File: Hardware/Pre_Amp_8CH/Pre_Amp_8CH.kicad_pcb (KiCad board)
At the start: 2 copper layers, 200 x 75 mm, 5 parts, among them J1 PJRAS4X2U01AUX, J2 PJRAS4X2U01AUX, J3 USB_C_Receptacle_PowerOnly_6P

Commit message: DSP start
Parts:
- added IC501: STA309A13TR, Pre_Amp_8CH_Footprints:QFP50P1200X1200X160-64N, F.Cu at (179.1, 120.0)
- added U601: STM32F410R8Tx, Package_QFP:LQFP-64_10x10mm_P0.5mm, F.Cu at (104.1, 120.0)
- renumbered J3 to J201, J1 to J301, J2 to J401, R1 to R201, R2 to R202
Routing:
- net /PSU/VBUS: track 0.00 -> 7.23 mm
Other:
- outline, holes or cut-outs redrawn

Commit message: PSU
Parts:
- added C201: 865060240001, Pre_Amp_8CH_Footprints:CP_Wurth_WCAP-ASLL-D4L5.5, F.Cu at (67.6, 97.3)
- added C202: 865060240001, Pre_Amp_8CH_Footprints:CP_Wurth_WCAP-ASLL-D4L5.5, F.Cu at (76.7, 107.9)
- added C501: 100nF, Capacitor_SMD:C_0603_1608Metric_Pad1.08x0.95mm_HandSolder, F.Cu at (183.0, 130.0)
- added C502: 1nF, Capacitor_SMD:C_0603_1608Metric_Pad1.08x0.95mm_HandSolder, F.Cu at (195.5, 131.6)
- added C503: 100nF, Capacitor_SMD:C_0603_1608Metric_Pad1.08x0.95mm_HandSolder, F.Cu at (168.8, 123.7)
- added C504: 100nF, Capacitor_SMD:C_0603_1608Metric_Pad1.08x0.95mm_HandSolder, F.Cu at (190.2, 122.7)
- added C505: 100nF, Capacitor_SMD:C_0603_1608Metric_Pad1.08x0.95mm_HandSolder, F.Cu at (189.9, 117.6)
- added C506: 100nF, Capacitor_SMD:C_0603_1608Metric_Pad1.08x0.95mm_HandSolder, F.Cu at (181.8, 109.7)
- added C507: 100nF, Capacitor_SMD:C_0603_1608Metric_Pad1.08x0.95mm_HandSolder, F.Cu at (177.2, 109.2)
- added C508: 1n2, Capacitor_SMD:C_0603_1608Metric_Pad1.08x0.95mm_HandSolder, F.Cu at (180.7, 137.8)
- added C509: 2u2, Capacitor_SMD:C_0805_2012Metric_Pad1.18x1.45mm_HandSolder, F.Cu at (168.5, 107.8)
- added C510: 100nF, Capacitor_SMD:C_0603_1608Metric_Pad1.08x0.95mm_HandSolder, F.Cu at (168.5, 110.8)
- added C511: 100p, Capacitor_SMD:C_0603_1608Metric_Pad1.08x0.95mm_HandSolder, F.Cu at (179.8, 133.7)
- added C512: 100p, Capacitor_SMD:C_0603_1608Metric_Pad1.08x0.95mm_HandSolder, F.Cu at (179.0, 128.7)
- added C513: 100nF, Capacitor_SMD:C_0603_1608Metric_Pad1.08x0.95mm_HandSolder, F.Cu at (205.1, 134.6)
- added C514: 47p, Capacitor_SMD:C_0603_1608Metric_Pad1.08x0.95mm_HandSolder, F.Cu at (165.8, 121.7)
- added C515: 1nF, Capacitor_SMD:C_0603_1608Metric_Pad1.08x0.95mm_HandSolder, F.Cu at (201.5, 122.7)
- added FB501: 600ohm100MHz, Resistor_SMD:R_0805_2012Metric_Pad1.20x1.40mm_HandSolder, F.Cu at (183.9, 136.8)
- added JP201: USB_jumper, Jumper:SolderJumper-2_P1.3mm_Open_Pad1.0x1.5mm, F.Cu at (65.8, 89.3)
- added JP202: 3V3_jumper, Jumper:SolderJumper-2_P1.3mm_Open_Pad1.0x1.5mm, F.Cu at (80.6, 113.2)
- added L201: BMRA000606301R0MA1, Pre_Amp_8CH_Footprints:INDPM7366X300N, F.Cu at (68.7, 109.7)
- added R203: 453k, Resistor_SMD:R_0603_1608Metric_Pad0.98x0.95mm_HandSolder, F.Cu at (72.8, 102.7)
- added R204: 100k, Resistor_SMD:R_0603_1608Metric_Pad0.98x0.95mm_HandSolder, F.Cu at (69.8, 102.7)
- added R501: 3K4, Resistor_SMD:R_0603_1608Metric_Pad0.98x0.95mm_HandSolder, F.Cu at (177.0, 133.7)
- added R502: 10K, Resistor_SMD:R_0603_1608Metric_Pad0.98x0.95mm_HandSolder, F.Cu at (168.1, 131.9)
- added R503: 10K, Resistor_SMD:R_0603_1608Metric_Pad0.98x0.95mm_HandSolder, F.Cu at (171.0, 131.9)
- added TP201: USB, TestPoint:TestPoint_Pad_D1.0mm, F.Cu at (65.8, 86.0)
- added TP202: 3V3, TestPoint:TestPoint_Pad_D1.0mm, F.Cu at (76.7, 113.2)
- added U201: TLV62569ADRL, Package_TO_SOT_SMD:SOT-563, F.Cu at (66.3, 104.2)
- R201, R202: footprint Resistor_SMD:R_0805_2012Metric_Pad1.20x1.40mm_HandSolder -> Resistor_SMD:R_0603_1608Metric_Pad0.98x0.95mm_HandSolder
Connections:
- IC501 pad 1: unconnected-(IC501-MVO-Pad1) -> +3V3
- IC501 pad 10: unconnected-(IC501-LRCKI-Pad10) -> /Audio_DSP/LRCKI
- IC501 pad 11: unconnected-(IC501-BICKI-Pad11) -> /Audio_DSP/BICKI
- IC501 pad 15: unconnected-(IC501-RESET-Pad15) -> /Audio_DSP/POWER_ON_RESET
- IC501 pad 16: unconnected-(IC501-PLLB-Pad16) -> GNDD
- IC501 pad 17: unconnected-(IC501-SA-Pad17) -> GNDD
- IC501 pad 20: unconnected-(IC501-XTI-Pad20) -> /Audio_DSP/MCLK
- IC501 pad 21: unconnected-(IC501-FILTER_PLL-Pad21) -> /Audio_DSP/PLL-Filter
- IC501 pad 23: unconnected-(IC501-GNDA-Pad23) -> /Audio_DSP/PLL-Filter-GND
- IC501 pad 24: unconnected-(IC501-VDDA-Pad24) -> Net-(IC501-VDDA)
- IC501 pad 25: unconnected-(IC501-CKOUT-Pad25) -> /Audio_DSP/CKOUT
- IC501 pad 29: unconnected-(IC501-OUT8_B-Pad29) -> /Audio_DSP/OUT8_B
- IC501 pad 30: unconnected-(IC501-OUT8_A-Pad30) -> /Audio_DSP/OUT8_A
- IC501 pad 31: unconnected-(IC501-OUT7_B-Pad31) -> /Audio_DSP/OUT7_B
- IC501 pad 32: unconnected-(IC501-OUT7_A-Pad32) -> /Audio_DSP/OUT7_A
- IC501 pad 33: unconnected-(IC501-OUT6_B-Pad33) -> /Audio_DSP/OUT6_B
- IC501 pad 34: unconnected-(IC501-OUT6_A-Pad34) -> /Audio_DSP/OUT6_A
- IC501 pad 38: unconnected-(IC501-OUT5_B-Pad38) -> /Audio_DSP/OUT5_B
- IC501 pad 39: unconnected-(IC501-OUT5_A-Pad39) -> /Audio_DSP/OUT5_A
- IC501 pad 40: unconnected-(IC501-OUT4_B-Pad40) -> /Audio_DSP/OUT4_B
- IC501 pad 41: unconnected-(IC501-OUT4_A-Pad41) -> /Audio_DSP/OUT4_A
- IC501 pad 42: unconnected-(IC501-OUT3_B-Pad42) -> /Audio_DSP/OUT3_B
- IC501 pad 43: unconnected-(IC501-OUT3_A-Pad43) -> /Audio_DSP/OUT3_A
- IC501 pad 47: unconnected-(IC501-OUT2_B-Pad47) -> /Audio_DSP/OUT2_B
- IC501 pad 48: unconnected-(IC501-OUT2_A-Pad48) -> /Audio_DSP/OUT2_A
- IC501 pad 49: unconnected-(IC501-OUT1_B-Pad49) -> /Audio_DSP/OUT1_B
- IC501 pad 50: unconnected-(IC501-OUT1_A-Pad50) -> /Audio_DSP/OUT1_A
- IC501 pad 51: unconnected-(IC501-EAPD-Pad51) -> /Audio_DSP/EAPD
- IC501 pad 55: unconnected-(IC501-BICKO-Pad55) -> /Audio_DSP/BICKO
- IC501 pad 56: unconnected-(IC501-LRCKO-Pad56) -> /Audio_DSP/LRCKO
- IC501 pad 57: unconnected-(IC501-SDO_12-Pad57) -> /Audio_DSP/SDATA_OUT_12
- IC501 pad 58: unconnected-(IC501-SDO_34-Pad58) -> /Audio_DSP/SDATA_OUT_34
- IC501 pad 6: unconnected-(IC501-SDI_78-Pad6) -> /Audio_DSP/SDATA_IN_78
- IC501 pad 62: unconnected-(IC501-SDO_56-Pad62) -> /Audio_DSP/SDATA_OUT_56
- IC501 pad 63: unconnected-(IC501-SDO_78-Pad63) -> /Audio_DSP/SDATA_OUT_78
- IC501 pad 64: unconnected-(IC501-PWDN-Pad64) -> /Audio_DSP/PWDN
- IC501 pad 7: unconnected-(IC501-SDI_56-Pad7) -> /Audio_DSP/SDATA_IN_56
- IC501 pad 8: unconnected-(IC501-SDI_34-Pad8) -> /Audio_DSP/SDATA_IN_34
- IC501 pad 9: unconnected-(IC501-SDI_12-Pad9) -> /Audio_DSP/SDATA_IN_12
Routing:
- net /Audio_DSP/I2C_SDA: track 0.00 -> 12.4 mm
- net /PSU/VBUS: track 7.23 -> 17.8 mm
- net /Audio_DSP/I2C_SCL: track 0.00 -> 9.84 mm
- net +5V: track 0.00 -> 8.98 mm
- net /PSU/FB: track 0.00 -> 7.03 mm
- net +3V3: track 0.00 -> 2.95 mm, vias 0 -> 4
- net GNDD: track 0.00 -> 2.31 mm, vias 2 -> 16
- added copper zone on F.Cu, net +5V
- added copper zone on F.Cu, net /PSU/3V3_sb
- added copper zone on F.Cu, net /PSU/SW
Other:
- outline, holes or cut-outs redrawn
- copper layers 2 -> 4

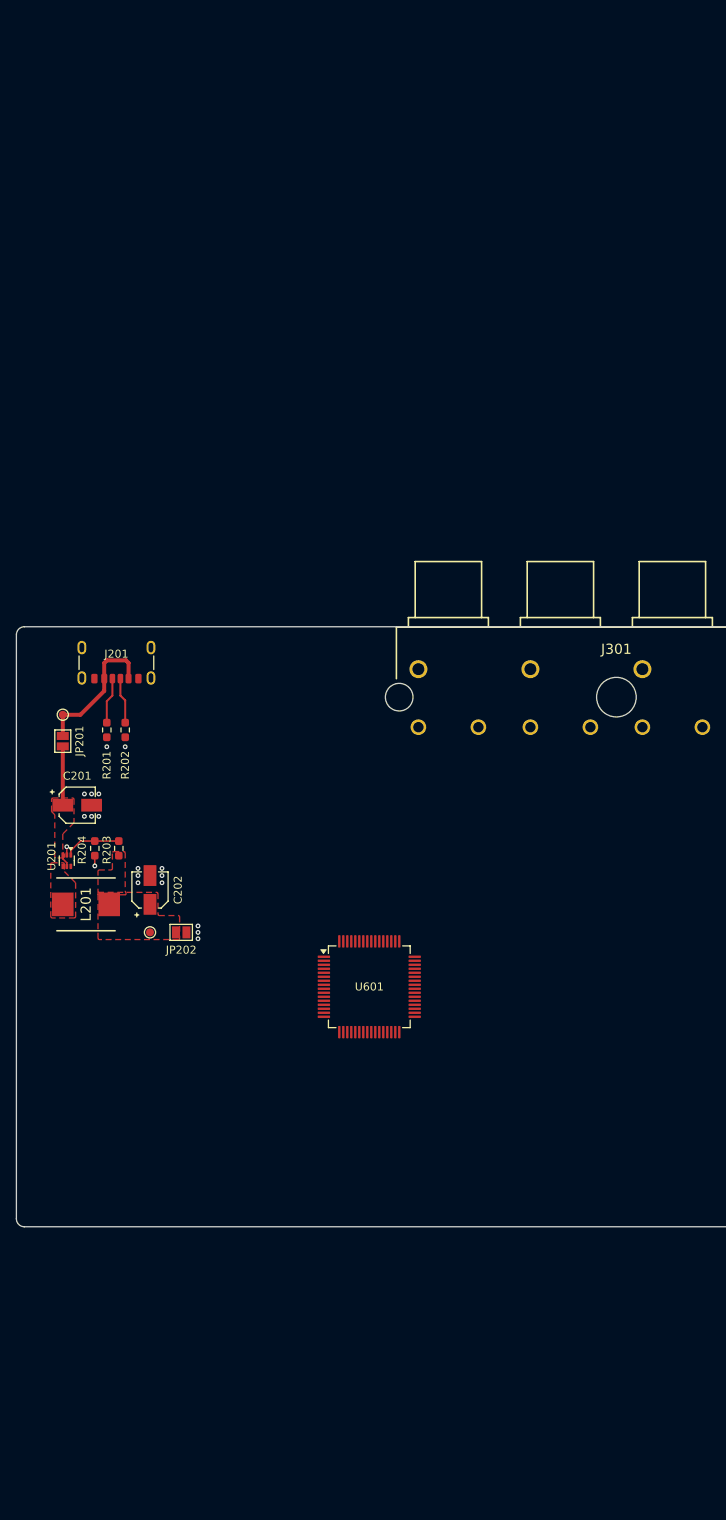
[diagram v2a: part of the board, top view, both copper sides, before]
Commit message: audio input buffers
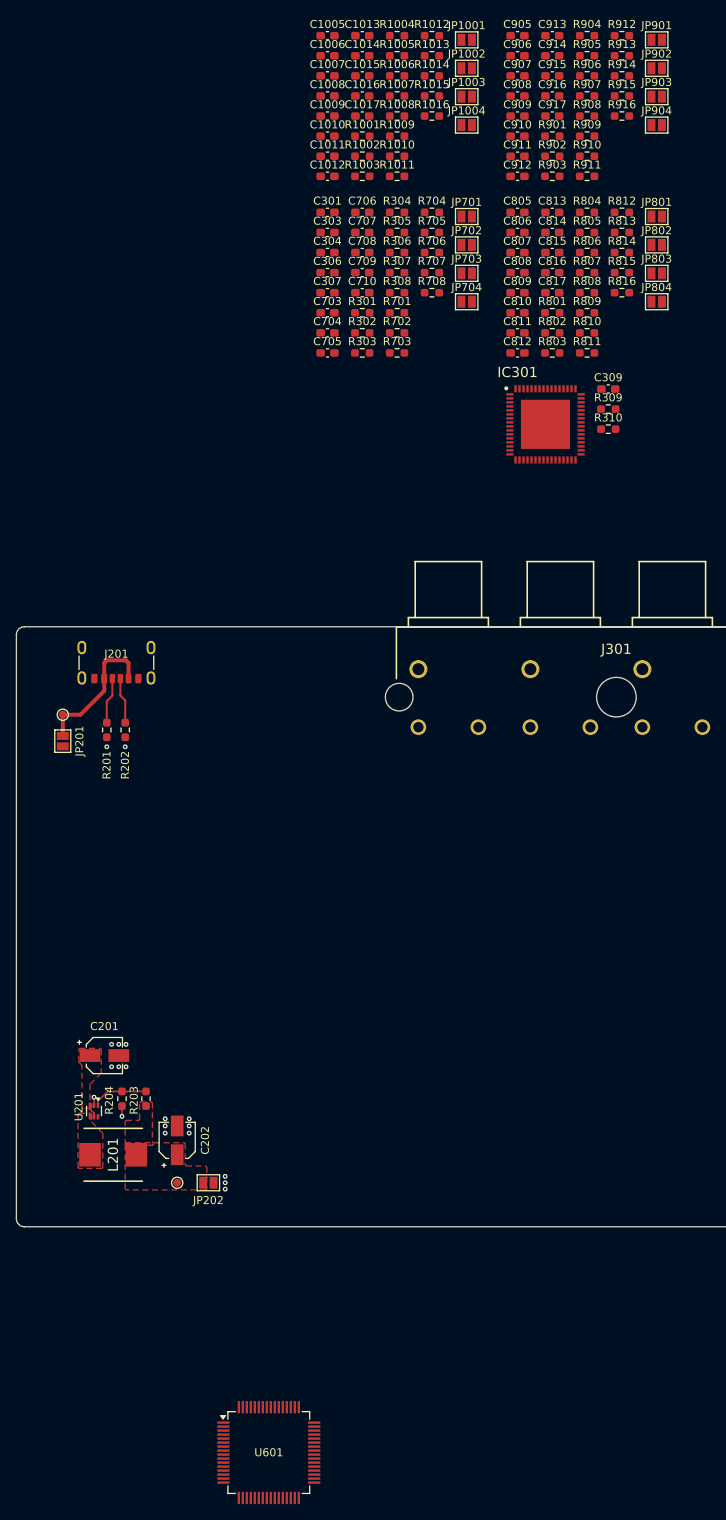
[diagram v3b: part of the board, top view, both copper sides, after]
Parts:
- added C1005: 1n_film, Capacitor_SMD:C_0603_1608Metric_Pad1.08x0.95mm_HandSolder, F.Cu at (98.9, 1.12)
- added C1006: 1n_film, Capacitor_SMD:C_0603_1608Metric_Pad1.08x0.95mm_HandSolder, F.Cu at (98.9, 3.63)
- added C1007: 1n_film, Capacitor_SMD:C_0603_1608Metric_Pad1.08x0.95mm_HandSolder, F.Cu at (98.9, 6.14)
- added C1008: 1n_film, Capacitor_SMD:C_0603_1608Metric_Pad1.08x0.95mm_HandSolder, F.Cu at (98.9, 8.65)
- added C1009: 100p, Capacitor_SMD:C_0603_1608Metric_Pad1.08x0.95mm_HandSolder, F.Cu at (98.9, 11.2)
- added C1010: 100p, Capacitor_SMD:C_0603_1608Metric_Pad1.08x0.95mm_HandSolder, F.Cu at (98.9, 13.7)
- added C1011: 100p, Capacitor_SMD:C_0603_1608Metric_Pad1.08x0.95mm_HandSolder, F.Cu at (98.9, 16.2)
- added C1012: 100p, Capacitor_SMD:C_0603_1608Metric_Pad1.08x0.95mm_HandSolder, F.Cu at (98.9, 18.7)
- added C1013: 15n_film, Capacitor_SMD:C_0603_1608Metric_Pad1.08x0.95mm_HandSolder, F.Cu at (103.2, 1.12)
- added C1014: 15n_film, Capacitor_SMD:C_0603_1608Metric_Pad1.08x0.95mm_HandSolder, F.Cu at (103.2, 3.63)
- added C1015: 100n, Capacitor_SMD:C_0603_1608Metric_Pad1.08x0.95mm_HandSolder, F.Cu at (103.2, 6.14)
- added C1016: 100n, Capacitor_SMD:C_0603_1608Metric_Pad1.08x0.95mm_HandSolder, F.Cu at (103.2, 8.65)
- added C1017: 100n, Capacitor_SMD:C_0603_1608Metric_Pad1.08x0.95mm_HandSolder, F.Cu at (103.2, 11.2)
- added C301: 1n_film, Capacitor_SMD:C_0603_1608Metric_Pad1.08x0.95mm_HandSolder, F.Cu at (98.9, 23.2)
- added C303: 100p, Capacitor_SMD:C_0603_1608Metric_Pad1.08x0.95mm_HandSolder, F.Cu at (98.9, 25.7)
- added C304: 15n_film, Capacitor_SMD:C_0603_1608Metric_Pad1.08x0.95mm_HandSolder, F.Cu at (98.9, 28.2)
- added C306: 1n_film, Capacitor_SMD:C_0603_1608Metric_Pad1.08x0.95mm_HandSolder, F.Cu at (98.9, 30.7)
- added C307: 100p, Capacitor_SMD:C_0603_1608Metric_Pad1.08x0.95mm_HandSolder, F.Cu at (98.9, 33.2)
- added C309: 100n, Capacitor_SMD:C_0603_1608Metric_Pad1.08x0.95mm_HandSolder, F.Cu at (134.0, 45.3)
- added C703: 1n_film, Capacitor_SMD:C_0603_1608Metric_Pad1.08x0.95mm_HandSolder, F.Cu at (98.9, 35.8)
- added C704: 1n_film, Capacitor_SMD:C_0603_1608Metric_Pad1.08x0.95mm_HandSolder, F.Cu at (98.9, 38.3)
- added C705: 100p, Capacitor_SMD:C_0603_1608Metric_Pad1.08x0.95mm_HandSolder, F.Cu at (98.9, 40.8)
- added C706: 100p, Capacitor_SMD:C_0603_1608Metric_Pad1.08x0.95mm_HandSolder, F.Cu at (103.2, 23.2)
- added C707: 15n_film, Capacitor_SMD:C_0603_1608Metric_Pad1.08x0.95mm_HandSolder, F.Cu at (103.2, 25.7)
- added C708: 100n, Capacitor_SMD:C_0603_1608Metric_Pad1.08x0.95mm_HandSolder, F.Cu at (103.2, 28.2)
- added C709: 100n, Capacitor_SMD:C_0603_1608Metric_Pad1.08x0.95mm_HandSolder, F.Cu at (103.2, 30.7)
- added C710: 100n, Capacitor_SMD:C_0603_1608Metric_Pad1.08x0.95mm_HandSolder, F.Cu at (103.2, 33.2)
- added C805: 1n_film, Capacitor_SMD:C_0603_1608Metric_Pad1.08x0.95mm_HandSolder, F.Cu at (122.6, 23.2)
- added C806: 1n_film, Capacitor_SMD:C_0603_1608Metric_Pad1.08x0.95mm_HandSolder, F.Cu at (122.6, 25.7)
- added C807: 1n_film, Capacitor_SMD:C_0603_1608Metric_Pad1.08x0.95mm_HandSolder, F.Cu at (122.6, 28.2)
- added C808: 1n_film, Capacitor_SMD:C_0603_1608Metric_Pad1.08x0.95mm_HandSolder, F.Cu at (122.6, 30.7)
- added C809: 100p, Capacitor_SMD:C_0603_1608Metric_Pad1.08x0.95mm_HandSolder, F.Cu at (122.6, 33.2)
- added C810: 100p, Capacitor_SMD:C_0603_1608Metric_Pad1.08x0.95mm_HandSolder, F.Cu at (122.6, 35.8)
- added C811: 100p, Capacitor_SMD:C_0603_1608Metric_Pad1.08x0.95mm_HandSolder, F.Cu at (122.6, 38.3)
- added C812: 100p, Capacitor_SMD:C_0603_1608Metric_Pad1.08x0.95mm_HandSolder, F.Cu at (122.6, 40.8)
- added C813: 15n_film, Capacitor_SMD:C_0603_1608Metric_Pad1.08x0.95mm_HandSolder, F.Cu at (127.0, 23.2)
- added C814: 15n_film, Capacitor_SMD:C_0603_1608Metric_Pad1.08x0.95mm_HandSolder, F.Cu at (127.0, 25.7)
- added C815: 100n, Capacitor_SMD:C_0603_1608Metric_Pad1.08x0.95mm_HandSolder, F.Cu at (127.0, 28.2)
- added C816: 100n, Capacitor_SMD:C_0603_1608Metric_Pad1.08x0.95mm_HandSolder, F.Cu at (127.0, 30.7)
- added C817: 100n, Capacitor_SMD:C_0603_1608Metric_Pad1.08x0.95mm_HandSolder, F.Cu at (127.0, 33.2)
- added C905: 1n_film, Capacitor_SMD:C_0603_1608Metric_Pad1.08x0.95mm_HandSolder, F.Cu at (122.6, 1.12)
- added C906: 1n_film, Capacitor_SMD:C_0603_1608Metric_Pad1.08x0.95mm_HandSolder, F.Cu at (122.6, 3.63)
- added C907: 1n_film, Capacitor_SMD:C_0603_1608Metric_Pad1.08x0.95mm_HandSolder, F.Cu at (122.6, 6.14)
- added C908: 1n_film, Capacitor_SMD:C_0603_1608Metric_Pad1.08x0.95mm_HandSolder, F.Cu at (122.6, 8.65)
- added C909: 100p, Capacitor_SMD:C_0603_1608Metric_Pad1.08x0.95mm_HandSolder, F.Cu at (122.6, 11.2)
- added C910: 100p, Capacitor_SMD:C_0603_1608Metric_Pad1.08x0.95mm_HandSolder, F.Cu at (122.6, 13.7)
- added C911: 100p, Capacitor_SMD:C_0603_1608Metric_Pad1.08x0.95mm_HandSolder, F.Cu at (122.6, 16.2)
- added C912: 100p, Capacitor_SMD:C_0603_1608Metric_Pad1.08x0.95mm_HandSolder, F.Cu at (122.6, 18.7)
- added C913: 15n_film, Capacitor_SMD:C_0603_1608Metric_Pad1.08x0.95mm_HandSolder, F.Cu at (127.0, 1.12)
- added C914: 15n_film, Capacitor_SMD:C_0603_1608Metric_Pad1.08x0.95mm_HandSolder, F.Cu at (127.0, 3.63)
- added C915: 100n, Capacitor_SMD:C_0603_1608Metric_Pad1.08x0.95mm_HandSolder, F.Cu at (127.0, 6.14)
- added C916: 100n, Capacitor_SMD:C_0603_1608Metric_Pad1.08x0.95mm_HandSolder, F.Cu at (127.0, 8.65)
- added C917: 100n, Capacitor_SMD:C_0603_1608Metric_Pad1.08x0.95mm_HandSolder, F.Cu at (127.0, 11.2)
- added IC301: AK5558VN, Pre_Amp_8CH_Footprints:QFN50P900X900X100-65N, F.Cu at (126.1, 49.7)
- added JP1001: SolderJumper_2_Open, Jumper:SolderJumper-2_P1.3mm_Open_Pad1.0x1.5mm, F.Cu at (116.3, 1.64)
- added JP1002: SolderJumper_2_Open, Jumper:SolderJumper-2_P1.3mm_Open_Pad1.0x1.5mm, F.Cu at (116.3, 5.19)
- added JP1003: SolderJumper_2_Open, Jumper:SolderJumper-2_P1.3mm_Open_Pad1.0x1.5mm, F.Cu at (116.3, 8.74)
- added JP1004: SolderJumper_2_Open, Jumper:SolderJumper-2_P1.3mm_Open_Pad1.0x1.5mm, F.Cu at (116.3, 12.3)
- added JP701: SolderJumper_2_Open, Jumper:SolderJumper-2_P1.3mm_Open_Pad1.0x1.5mm, F.Cu at (116.3, 23.7)
- added JP702: SolderJumper_2_Open, Jumper:SolderJumper-2_P1.3mm_Open_Pad1.0x1.5mm, F.Cu at (116.3, 27.3)
- added JP703: SolderJumper_2_Open, Jumper:SolderJumper-2_P1.3mm_Open_Pad1.0x1.5mm, F.Cu at (116.3, 30.8)
- added JP704: SolderJumper_2_Open, Jumper:SolderJumper-2_P1.3mm_Open_Pad1.0x1.5mm, F.Cu at (116.3, 34.4)
- added JP801: SolderJumper_2_Open, Jumper:SolderJumper-2_P1.3mm_Open_Pad1.0x1.5mm, F.Cu at (140.0, 23.7)
- added JP802: SolderJumper_2_Open, Jumper:SolderJumper-2_P1.3mm_Open_Pad1.0x1.5mm, F.Cu at (140.0, 27.3)
- added JP803: SolderJumper_2_Open, Jumper:SolderJumper-2_P1.3mm_Open_Pad1.0x1.5mm, F.Cu at (140.0, 30.8)
- added JP804: SolderJumper_2_Open, Jumper:SolderJumper-2_P1.3mm_Open_Pad1.0x1.5mm, F.Cu at (140.0, 34.4)
- added JP901: SolderJumper_2_Open, Jumper:SolderJumper-2_P1.3mm_Open_Pad1.0x1.5mm, F.Cu at (140.0, 1.64)
- added JP902: SolderJumper_2_Open, Jumper:SolderJumper-2_P1.3mm_Open_Pad1.0x1.5mm, F.Cu at (140.0, 5.19)
- added JP903: SolderJumper_2_Open, Jumper:SolderJumper-2_P1.3mm_Open_Pad1.0x1.5mm, F.Cu at (140.0, 8.74)
- added JP904: SolderJumper_2_Open, Jumper:SolderJumper-2_P1.3mm_Open_Pad1.0x1.5mm, F.Cu at (140.0, 12.3)
- added R1001: 4K7, Resistor_SMD:R_0603_1608Metric_Pad0.98x0.95mm_HandSolder, F.Cu at (103.2, 13.7)
- added R1002: 4K7, Resistor_SMD:R_0603_1608Metric_Pad0.98x0.95mm_HandSolder, F.Cu at (103.2, 16.2)
- added R1003: 4K7, Resistor_SMD:R_0603_1608Metric_Pad0.98x0.95mm_HandSolder, F.Cu at (103.2, 18.7)
- added R1004: 4K7, Resistor_SMD:R_0603_1608Metric_Pad0.98x0.95mm_HandSolder, F.Cu at (107.6, 1.12)
- added R1005: 3K3, Resistor_SMD:R_0603_1608Metric_Pad0.98x0.95mm_HandSolder, F.Cu at (107.6, 3.63)
- added R1006: 3K3, Resistor_SMD:R_0603_1608Metric_Pad0.98x0.95mm_HandSolder, F.Cu at (107.6, 6.14)
- added R1007: 3K3, Resistor_SMD:R_0603_1608Metric_Pad0.98x0.95mm_HandSolder, F.Cu at (107.6, 8.65)
- added R1008: 3K3, Resistor_SMD:R_0603_1608Metric_Pad0.98x0.95mm_HandSolder, F.Cu at (107.6, 11.2)
- added R1009: 3K3, Resistor_SMD:R_0603_1608Metric_Pad0.98x0.95mm_HandSolder, F.Cu at (107.6, 13.7)
- added R1010: 3K3, Resistor_SMD:R_0603_1608Metric_Pad0.98x0.95mm_HandSolder, F.Cu at (107.6, 16.2)
- added R1011: 3K3, Resistor_SMD:R_0603_1608Metric_Pad0.98x0.95mm_HandSolder, F.Cu at (107.6, 18.7)
- added R1012: 3K3, Resistor_SMD:R_0603_1608Metric_Pad0.98x0.95mm_HandSolder, F.Cu at (111.9, 1.12)
- added R1013: 10E, Resistor_SMD:R_0603_1608Metric_Pad0.98x0.95mm_HandSolder, F.Cu at (111.9, 3.63)
- added R1014: 10E, Resistor_SMD:R_0603_1608Metric_Pad0.98x0.95mm_HandSolder, F.Cu at (111.9, 6.14)
- added R1015: 10E, Resistor_SMD:R_0603_1608Metric_Pad0.98x0.95mm_HandSolder, F.Cu at (111.9, 8.65)
- added R1016: 10E, Resistor_SMD:R_0603_1608Metric_Pad0.98x0.95mm_HandSolder, F.Cu at (111.9, 11.2)
- added R301: 4K7, Resistor_SMD:R_0603_1608Metric_Pad0.98x0.95mm_HandSolder, F.Cu at (103.2, 35.8)
- added R302: 4K7, Resistor_SMD:R_0603_1608Metric_Pad0.98x0.95mm_HandSolder, F.Cu at (103.2, 38.3)
- added R303: 3K3, Resistor_SMD:R_0603_1608Metric_Pad0.98x0.95mm_HandSolder, F.Cu at (103.2, 40.8)
- added R304: 3K3, Resistor_SMD:R_0603_1608Metric_Pad0.98x0.95mm_HandSolder, F.Cu at (107.6, 23.2)
- added R305: 10E, Resistor_SMD:R_0603_1608Metric_Pad0.98x0.95mm_HandSolder, F.Cu at (107.6, 25.7)
- added R306: 3K3, Resistor_SMD:R_0603_1608Metric_Pad0.98x0.95mm_HandSolder, F.Cu at (107.6, 28.2)
- added R307: 3K3, Resistor_SMD:R_0603_1608Metric_Pad0.98x0.95mm_HandSolder, F.Cu at (107.6, 30.7)
- added R308: 10E, Resistor_SMD:R_0603_1608Metric_Pad0.98x0.95mm_HandSolder, F.Cu at (107.6, 33.2)
- added R309: 10K, Resistor_SMD:R_0603_1608Metric_Pad0.98x0.95mm_HandSolder, F.Cu at (134.0, 47.8)
- added R310: 10K, Resistor_SMD:R_0603_1608Metric_Pad0.98x0.95mm_HandSolder, F.Cu at (134.0, 50.3)
- added R701: 4K7, Resistor_SMD:R_0603_1608Metric_Pad0.98x0.95mm_HandSolder, F.Cu at (107.6, 35.8)
- added R702: 4K7, Resistor_SMD:R_0603_1608Metric_Pad0.98x0.95mm_HandSolder, F.Cu at (107.6, 38.3)
- added R703: 3K3, Resistor_SMD:R_0603_1608Metric_Pad0.98x0.95mm_HandSolder, F.Cu at (107.6, 40.8)
- added R704: 3K3, Resistor_SMD:R_0603_1608Metric_Pad0.98x0.95mm_HandSolder, F.Cu at (111.9, 23.2)
- added R705: 3K3, Resistor_SMD:R_0603_1608Metric_Pad0.98x0.95mm_HandSolder, F.Cu at (111.9, 25.7)
- added R706: 3K3, Resistor_SMD:R_0603_1608Metric_Pad0.98x0.95mm_HandSolder, F.Cu at (111.9, 28.2)
- added R707: 10E, Resistor_SMD:R_0603_1608Metric_Pad0.98x0.95mm_HandSolder, F.Cu at (111.9, 30.7)
- added R708: 10E, Resistor_SMD:R_0603_1608Metric_Pad0.98x0.95mm_HandSolder, F.Cu at (111.9, 33.2)
- added R801: 4K7, Resistor_SMD:R_0603_1608Metric_Pad0.98x0.95mm_HandSolder, F.Cu at (127.0, 35.8)
- added R802: 4K7, Resistor_SMD:R_0603_1608Metric_Pad0.98x0.95mm_HandSolder, F.Cu at (127.0, 38.3)
- added R803: 4K7, Resistor_SMD:R_0603_1608Metric_Pad0.98x0.95mm_HandSolder, F.Cu at (127.0, 40.8)
- added R804: 4K7, Resistor_SMD:R_0603_1608Metric_Pad0.98x0.95mm_HandSolder, F.Cu at (131.3, 23.2)
- added R805: 3K3, Resistor_SMD:R_0603_1608Metric_Pad0.98x0.95mm_HandSolder, F.Cu at (131.3, 25.7)
- added R806: 3K3, Resistor_SMD:R_0603_1608Metric_Pad0.98x0.95mm_HandSolder, F.Cu at (131.3, 28.2)
- added R807: 3K3, Resistor_SMD:R_0603_1608Metric_Pad0.98x0.95mm_HandSolder, F.Cu at (131.3, 30.7)
- added R808: 3K3, Resistor_SMD:R_0603_1608Metric_Pad0.98x0.95mm_HandSolder, F.Cu at (131.3, 33.2)
- added R809: 3K3, Resistor_SMD:R_0603_1608Metric_Pad0.98x0.95mm_HandSolder, F.Cu at (131.3, 35.8)
- added R810: 3K3, Resistor_SMD:R_0603_1608Metric_Pad0.98x0.95mm_HandSolder, F.Cu at (131.3, 38.3)
- added R811: 3K3, Resistor_SMD:R_0603_1608Metric_Pad0.98x0.95mm_HandSolder, F.Cu at (131.3, 40.8)
- added R812: 3K3, Resistor_SMD:R_0603_1608Metric_Pad0.98x0.95mm_HandSolder, F.Cu at (135.7, 23.2)
- added R813: 10E, Resistor_SMD:R_0603_1608Metric_Pad0.98x0.95mm_HandSolder, F.Cu at (135.7, 25.7)
- added R814: 10E, Resistor_SMD:R_0603_1608Metric_Pad0.98x0.95mm_HandSolder, F.Cu at (135.7, 28.2)
- added R815: 10E, Resistor_SMD:R_0603_1608Metric_Pad0.98x0.95mm_HandSolder, F.Cu at (135.7, 30.7)
- added R816: 10E, Resistor_SMD:R_0603_1608Metric_Pad0.98x0.95mm_HandSolder, F.Cu at (135.7, 33.2)
- added R901: 4K7, Resistor_SMD:R_0603_1608Metric_Pad0.98x0.95mm_HandSolder, F.Cu at (127.0, 13.7)
- added R902: 4K7, Resistor_SMD:R_0603_1608Metric_Pad0.98x0.95mm_HandSolder, F.Cu at (127.0, 16.2)
- added R903: 4K7, Resistor_SMD:R_0603_1608Metric_Pad0.98x0.95mm_HandSolder, F.Cu at (127.0, 18.7)
- added R904: 4K7, Resistor_SMD:R_0603_1608Metric_Pad0.98x0.95mm_HandSolder, F.Cu at (131.3, 1.12)
- added R905: 3K3, Resistor_SMD:R_0603_1608Metric_Pad0.98x0.95mm_HandSolder, F.Cu at (131.3, 3.63)
- added R906: 3K3, Resistor_SMD:R_0603_1608Metric_Pad0.98x0.95mm_HandSolder, F.Cu at (131.3, 6.14)
- added R907: 3K3, Resistor_SMD:R_0603_1608Metric_Pad0.98x0.95mm_HandSolder, F.Cu at (131.3, 8.65)
- added R908: 3K3, Resistor_SMD:R_0603_1608Metric_Pad0.98x0.95mm_HandSolder, F.Cu at (131.3, 11.2)
- added R909: 3K3, Resistor_SMD:R_0603_1608Metric_Pad0.98x0.95mm_HandSolder, F.Cu at (131.3, 13.7)
- added R910: 3K3, Resistor_SMD:R_0603_1608Metric_Pad0.98x0.95mm_HandSolder, F.Cu at (131.3, 16.2)
- added R911: 3K3, Resistor_SMD:R_0603_1608Metric_Pad0.98x0.95mm_HandSolder, F.Cu at (131.3, 18.7)
- added R912: 3K3, Resistor_SMD:R_0603_1608Metric_Pad0.98x0.95mm_HandSolder, F.Cu at (135.7, 1.12)
- added R913: 10E, Resistor_SMD:R_0603_1608Metric_Pad0.98x0.95mm_HandSolder, F.Cu at (135.7, 3.63)
- added R914: 10E, Resistor_SMD:R_0603_1608Metric_Pad0.98x0.95mm_HandSolder, F.Cu at (135.7, 6.14)
- added R915: 10E, Resistor_SMD:R_0603_1608Metric_Pad0.98x0.95mm_HandSolder, F.Cu at (135.7, 8.65)
- added R916: 10E, Resistor_SMD:R_0603_1608Metric_Pad0.98x0.95mm_HandSolder, F.Cu at (135.7, 11.2)
- moved U601 59.6 mm to (91.5, 178.2)
- moved C201 31.5 mm to (71.0, 128.6)
- moved JP202 31.5 mm to (84.0, 144.5)
- moved L201 31.5 mm to (72.1, 141.0)
- moved R203 31.5 mm to (76.2, 134.0)
- moved R204 31.5 mm to (73.2, 134.0)
- moved TP202 31.5 mm to (80.1, 144.5)
- moved U201 31.5 mm to (69.7, 135.5)
- moved C202 31.5 mm to (80.1, 139.2)
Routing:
- net +5V: track 8.98 -> 1.63 mm
